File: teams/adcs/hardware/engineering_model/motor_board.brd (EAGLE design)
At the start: 90 x 90 mm, 67 parts

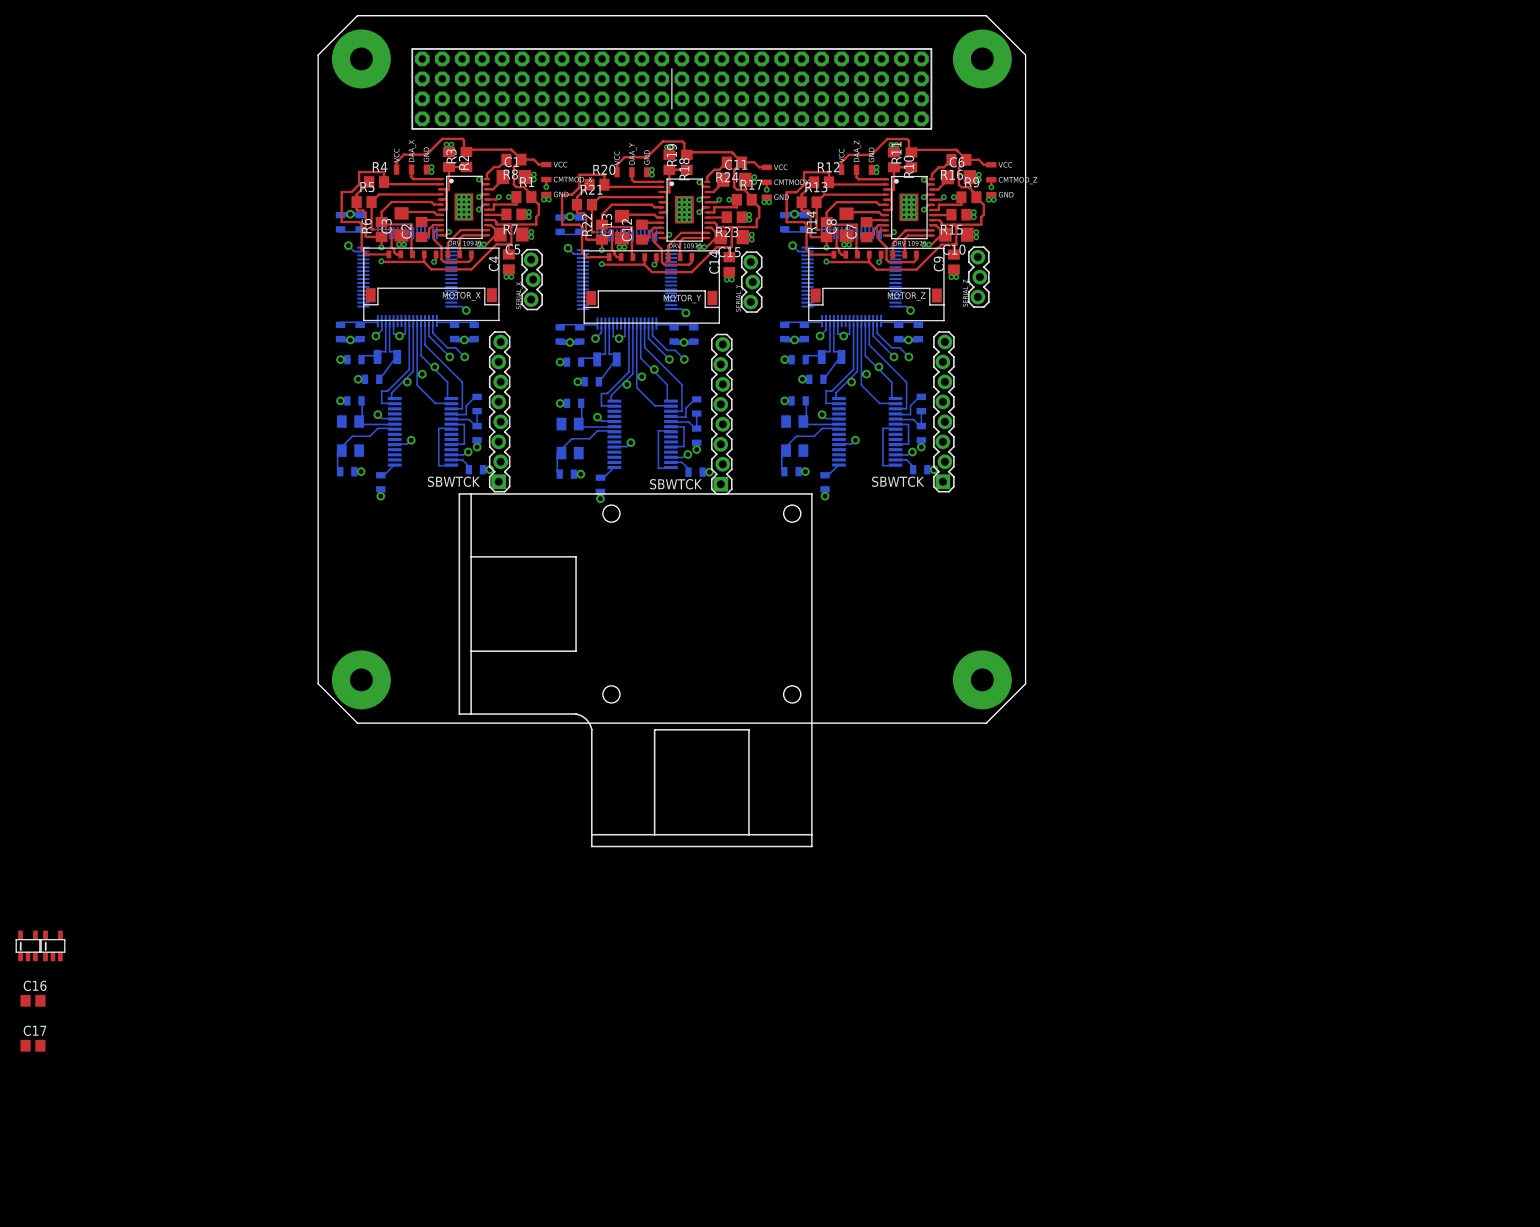
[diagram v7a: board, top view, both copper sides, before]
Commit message: ADCS/RW: Routed everything but SEPIC
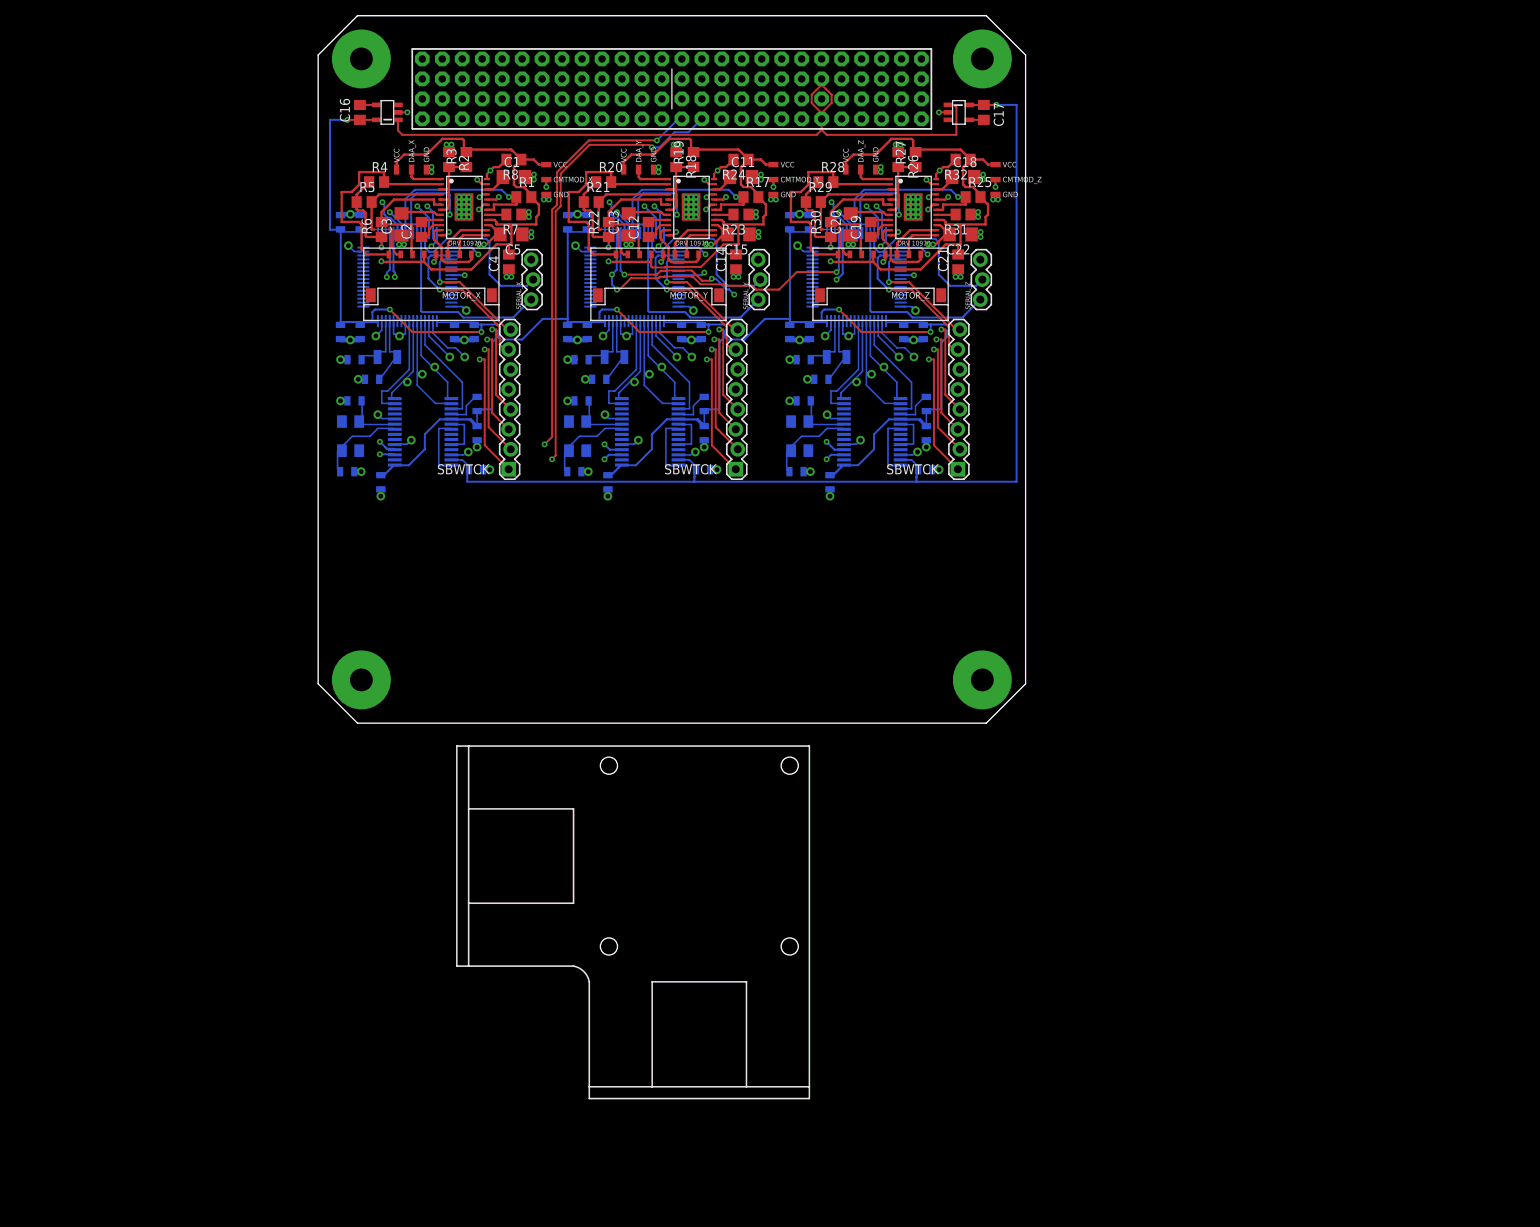
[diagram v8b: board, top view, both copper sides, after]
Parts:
- removed C10, C8: 1uF, rcl:C1206
- removed C6: 2.2uF, rcl:C1206
- removed C7, C9: 0.1uF, rcl:C0805
- removed CMTMODY: 0_OHM_JUMPER, DubSat1 Components:0_OHM_JUMPER
- removed R10, R11, R16, R9: 3.3K, rcl:R0805
- removed R12, R13, R14: 10K, rcl:R0805
- removed R15: (no value), rcl:R0805
- removed U$5, U$8: MSP-CAN_BLOCK, DubSat1 Components:MSP-CAN_BLOCK
- removed U$6: PROGRAM/DEBUG_PORT, DubSat1 Components:1X08_CONNECTOR
- added C18: 2.2uF, rcl:C1206
- added C19, C21: 0.1uF, rcl:C0805
- added C20, C22: 1uF, rcl:C1206
- added CMTMOD_Y: 0_OHM_JUMPER, DubSat1 Components:0_OHM_JUMPER
- added R25, R26, R27, R32: 3.3K, rcl:R0805
- added R28, R29, R30: 10K, rcl:R0805
- added R31: (no value), rcl:R0805
- added U$12, U$15: DRV10970, DubSat1 Components:DRV10970
- added U$14: PROGRAM/DEBUG_PORT, DubSat1 Components:1X08_CONNECTOR
- U$10, U$13: value DRV10970 -> MSP-CAN_BLOCK; device DubSat1 Components:DRV10970 -> DubSat1 Components:MSP-CAN_BLOCK
- moved C17 169.5 mm to (85.4, 78.4), turned to 270 degrees
- moved LDO_5V 159.0 mm to (82.2, 78.4), turned to 270 degrees
- moved C16 120.4 mm to (6.03, 78.4), turned to 90 degrees
- moved LDO_3V3 114.3 mm to (9.53, 78.4), turned to 90 degrees
- moved U$10 36.0 mm to (41.0, 57.5), flipped to the bottom, turned to 180 degrees
- moved U$9 32.1 mm to (49.2, -16.2)
- moved U$11 26.4 mm to (54.0, 33.0)
- moved U$13 23.5 mm to (69.2, 57.5), flipped to the bottom, turned to 180 degrees
- moved U$4 2.03 mm to (25.1, 33.0)
- moved SERIAL_Y 1.00 mm to (56.8, 54.6)
- moved C11 0.92 mm to (54.5, 70.2)
- moved C12 0.92 mm to (42.8, 63.5)
- moved R22 0.92 mm to (37.7, 63.5)
- moved C14 0.92 mm to (53.9, 59.4)
- moved DAA_Y 0.92 mm to (41.5, 71.1)
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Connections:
- net N$1 renamed SBWTCK_X
- net N$2 renamed SBWTDIO_X
- net N$3 renamed TXD_X
- net N$4 renamed RXD_X
- net N$5 renamed GPIO_DEBUG_3.4_X
- net N$6 renamed GPIO_DEBUG_3.5_X
- removed net FG: U$8.P7.4_GPIO
- removed net FR: U$8.P7.3_GPIO
- removed net N$10: U$5.P2.1_RXD, U$6.4
- removed net N$11: U$5.P3.4_GPIO_DEBUG, U$6.7
- removed net N$12: U$5.P3.5_GPIO_DEBUG, U$6.8
- removed net N$63: U$11.SBWTCK, U$8.SBWTCK
- removed net N$64: U$11.2, U$8.SBWTDIO
- removed net N$65: U$11.3, U$8.P2.0_TXD
- removed net N$66: U$11.4, U$8.P2.1_RXD
- removed net N$67: U$11.7, U$8.P3.4_GPIO_DEBUG
- removed net N$68: U$11.8, U$8.P3.5_GPIO_DEBUG
- removed net N$7: U$5.SBWTCK, U$6.SBWTCK
- removed net N$8: U$5.SBWTDIO, U$6.2
- removed net N$9: U$5.P2.0_TXD, U$6.3
- removed net PWM: U$8.P1.7_GPIO/PWM
- removed net RD: U$8.P4.0_GPIO
- removed net RETRY_Z_Y: C11.1, U$13.RETRY
- removed net V1_Z: MOTOR_Z.P$2, U$10.V
- removed net VM_Z: C10.2, U$10.VM
- new net GPIO_DEBUG_3.4_Y: U$10.P3.4_GPIO_DEBUG, U$11.7
- new net GPIO_DEBUG_3.4_Z: U$13.P3.4_GPIO_DEBUG, U$14.7
- new net GPIO_DEBUG_3.5_Y: U$10.P3.5_GPIO_DEBUG, U$11.8
- new net GPIO_DEBUG_3.5_Z: U$13.P3.5_GPIO_DEBUG, U$14.8
- new net RETRY_Y: C11.1, U$12.RETRY
- new net RXD_Y: U$10.P2.1_RXD, U$11.4
- new net RXD_Z: U$13.P2.1_RXD, U$14.4
- new net SBWTCK_Y: U$10.SBWTCK, U$11.SBWTCK
- new net SBWTCK_Z: U$13.SBWTCK, U$14.SBWTCK
- new net SBWTDIO_Y: U$10.SBWTDIO, U$11.2
- new net SBWTDIO_Z: U$13.SBWTDIO, U$14.2
- new net TXD_Y: U$10.P2.0_TXD, U$11.3
- new net TXD_Z: U$13.P2.0_TXD, U$14.3
- new net V_Z: MOTOR_Z.P$2, U$15.V
- net +3V3: now also U$10.3.3V@CAN1, U$10.3.3V@CAN2, U$10.3.3V@MSP1, U$10.3.3V@MSP2, U$10.3.3V_ANALOG@MSP2, U$13.3.3V@CAN1, U$13.3.3V@CAN2, U$13.3.3V@MSP1, U$13.3.3V@MSP2, U$13.3.3V_ANALOG@MSP2
- net +5V: now also U$10.5V, U$13.5V
- net BRKMOD_X: now also U$3.P4.3_GPIO
- net BRKMOD_Y: now also U$10.P4.3_GPIO, U$12.BRKMOD; no longer U$13.BRKMOD
- net BRKMOD_Z: now also U$13.P4.3_GPIO, U$15.BRKMOD; no longer U$10.BRKMOD
- net CANH: now also U$10.CANH, U$13.CANH; no longer U$5.CANH, U$8.CANH
- net CANL: now also U$10.CANL, U$13.CANL; no longer U$5.CANL, U$8.CANL
- net CMTMOD_Y: now also CMTMOD_Y.P$2, U$12.CMTMOD; no longer CMTMODY.P$2, U$13.CMTMOD
- net CMTMOD_Z: now also U$15.CMTMOD; no longer U$10.CMTMOD
- net CPN_Y: now also U$12.CPN; no longer U$13.CPN
- net CPN_Z: now also C19.1, U$15.CPN; no longer C7.1, U$10.CPN
- net CPP_Y: now also U$12.CPP; no longer U$13.CPP
- net CPP_Z: now also C19.2, U$15.CPP; no longer C7.2, U$10.CPP
- net CS_Y: now also U$12.CS; no longer U$13.CS
- net CS_Z: now also R31.2, U$15.CS; no longer R15.2, U$10.CS
- net DAA_Y: now also U$12.DAA; no longer U$13.DAA
- net DAA_Z: now also U$15.DAA; no longer U$10.DAA
- net FG_Y: now also U$10.P7.4_GPIO, U$12.FG; no longer U$13.FG, U$5.P7.4_GPIO
- net FG_Z: now also R32.2, U$13.P7.4_GPIO, U$15.FG; no longer R16.2, U$10.FG
- net FR_Y: now also U$10.P7.3_GPIO, U$12.FR; no longer U$13.FR, U$5.P7.3_GPIO
- net FR_Z: now also U$13.P7.3_GPIO, U$15.FR; no longer U$10.FR
- net GND: now also C18.2, C20.1, C21.1, C22.1, CMTMOD_Y.P$1, R26.1, R31.1, U$10.GND@10, U$10.GND@11, U$10.GND@12, U$10.GND@13, U$10.GND@14, U$10.GND@15, U$10.GND@16, U$10.GND@17, U$10.GND@26, U$10.GND@3, U$10.GND@4, U$10.GND@5, U$10.GND@7, U$10.GND@8, U$10.GND@9, U$12.GND@1, U$12.GND@2, U$13.GND@10, U$13.GND@11, U$13.GND@12, U$13.GND@13, U$13.GND@14, U$13.GND@15, U$13.GND@16, U$13.GND@17, U$13.GND@26, U$13.GND@3, U$13.GND@4, U$13.GND@5, U$13.GND@7, U$13.GND@8, U$13.GND@9, U$14.5, U$14.6, U$15.GND@1, U$15.GND@2; no longer C10.1, C6.2, C8.1, C9.1, CMTMODY.P$1, R10.1, R15.1, U$5.GND@1, U$5.GND@10, U$5.GND@11, U$5.GND@12, U$5.GND@13, U$5.GND@14, U$5.GND@15, U$5.GND@16, U$5.GND@17, U$5.GND@2, U$5.GND@26, U$5.GND@3, U$5.GND@4, U$5.GND@5, U$5.GND@7, U$5.GND@8, U$5.GND@9, U$6.5, U$6.6, U$8.GND@1, U$8.GND@10, U$8.GND@11, U$8.GND@12, U$8.GND@13, U$8.GND@14, U$8.GND@15, U$8.GND@16, U$8.GND@17, U$8.GND@2, U$8.GND@26, U$8.GND@3, U$8.GND@4, U$8.GND@5, U$8.GND@7, U$8.GND@8, U$8.GND@9
- net HN_Y: now also U$12.U_HN, U$12.V_HN, U$12.W_HN; no longer U$13.U_HN, U$13.V_HN, U$13.W_HN
- net HN_Z: now also R26.2, R27.1, U$15.U_HN, U$15.V_HN, U$15.W_HN; no longer R10.2, R11.1, U$10.U_HN, U$10.V_HN, U$10.W_HN
- net HP_U_Y: now also U$12.U_HP; no longer U$13.U_HP
- net HP_U_Z: now also R28.2, U$15.U_HP; no longer R12.2, U$10.U_HP
- net HP_V_Y: now also U$12.V_HP; no longer U$13.V_HP
- net HP_V_Z: now also R29.2, U$15.V_HP; no longer R13.2, U$10.V_HP
- net HP_W_Y: now also U$12.W_HP; no longer U$13.W_HP
- net HP_W_Z: now also R30.2, U$15.W_HP; no longer R14.2, U$10.W_HP
- net M_Y_RX: now also U$10.P2.6_GPIO/PWM; no longer U$5.P2.6_GPIO/PWM
- net M_Y_TX: now also U$10.P2.5_GPIO; no longer U$5.P2.5_GPIO
- net M_Z_RX: now also U$13.P2.6_GPIO/PWM; no longer U$8.P2.6_GPIO/PWM
- net M_Z_TX: now also U$13.P2.5_GPIO; no longer U$8.P2.5_GPIO
- net PWM_Y: now also U$10.P1.7_GPIO/PWM, U$12.PWM; no longer U$13.PWM, U$5.P1.7_GPIO/PWM
- net PWM_Z: now also U$13.P1.7_GPIO/PWM, U$15.PWM; no longer U$10.PWM
- net RD_Y: now also U$10.P4.0_GPIO, U$12.RD; no longer U$13.RD, U$5.P4.0_GPIO
- net RD_Z: now also R25.1, U$13.P4.0_GPIO, U$15.RD; no longer R9.1, U$10.RD
- net RETRY_Z: now also C18.1, U$15.RETRY; no longer C6.1, U$10.RETRY
- net SYNC1: now also U$10.P7.2_SYNC1, U$13.P7.2_SYNC1; no longer U$5.P7.2_SYNC1, U$8.P7.2_SYNC1
- net SYNC2: now also U$10.PJ.3_SYNC2, U$13.PJ.3_SYNC2; no longer U$5.PJ.3_SYNC2, U$8.PJ.3_SYNC2
- net U_Y: now also U$12.U; no longer U$13.U
- net U_Z: now also U$15.U; no longer U$10.U
- net VCP_Y: now also U$12.VCP; no longer U$13.VCP
- net VCP_Z: now also C20.2, U$15.VCP; no longer C8.2, U$10.VCP
- net VINT_Y: now also CMTMOD_Y.P$3, U$12.VINT; no longer CMTMODY.P$3, U$13.VINT
- net VINT_Z: now also C21.2, R25.2, R27.2, R28.1, R29.1, R30.1, R32.1, U$15.VINT; no longer C9.2, R11.2, R12.1, R13.1, R14.1, R16.1, R9.2, U$10.VINT
- net VM: now also C22.2, U$12.VM, U$15.VM; no longer U$13.VM
- net V_Y: now also U$12.V; no longer U$13.V
- net W_Y: now also U$12.W; no longer U$13.W
- net W_Z: now also U$15.W; no longer U$10.W
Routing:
- net +3V3: track 0.00 -> 243.7 mm, vias 0 -> 7
- net +5V: track 0.00 -> 128.5 mm, vias 0 -> 1
- net CANL: track 0.00 -> 121.8 mm, vias 0 -> 5
- net CANH: track 0.00 -> 120.0 mm, vias 0 -> 5
- net SYNC2: track 0.00 -> 116.6 mm, vias 0 -> 4
- net SYNC1: track 0.00 -> 114.2 mm, vias 0 -> 5
- net VBAT: track 0.00 -> 90.0 mm
- net SBWTCK_Z: track 0.00 -> 44.8 mm, vias 0 -> 2
- net SBWTCK_Y: track 0.00 -> 44.8 mm, vias 0 -> 2
- net SBWTCK_X: track 0.00 -> 44.8 mm, vias 0 -> 2
- net SBWTDIO_Y: track 0.00 -> 41.3 mm, vias 0 -> 2
- net SBWTDIO_Z: track 0.00 -> 41.3 mm, vias 0 -> 2
- net SBWTDIO_X: track 0.00 -> 41.3 mm, vias 0 -> 2
- net TXD_Y: track 0.00 -> 30.8 mm, vias 0 -> 2
- net TXD_X: track 0.00 -> 30.8 mm, vias 0 -> 2
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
